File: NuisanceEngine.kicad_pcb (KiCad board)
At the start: 2 copper layers, 60 x 50 mm, 63 parts, among them J1 GND, J2 CV, J3 9V, J4 GND, J5 BAT, J6 L, J7 R, J8 GND, Q1 2N3904, Q2 2N3904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

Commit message: Changed speaker connection
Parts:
- removed LS1: Speaker, Connectors_Molex:Molex_NanoFit_1x02x2.50mm_Straight
- added J10: S-, Connector_PinHeader_2.54mm:PinHeader_1x01_P2.54mm_Vertical, F.Cu at (154.5, 36.8)
- added J9: S+, Connector_PinHeader_2.54mm:PinHeader_1x01_P2.54mm_Vertical, F.Cu at (150.8, 36.8)

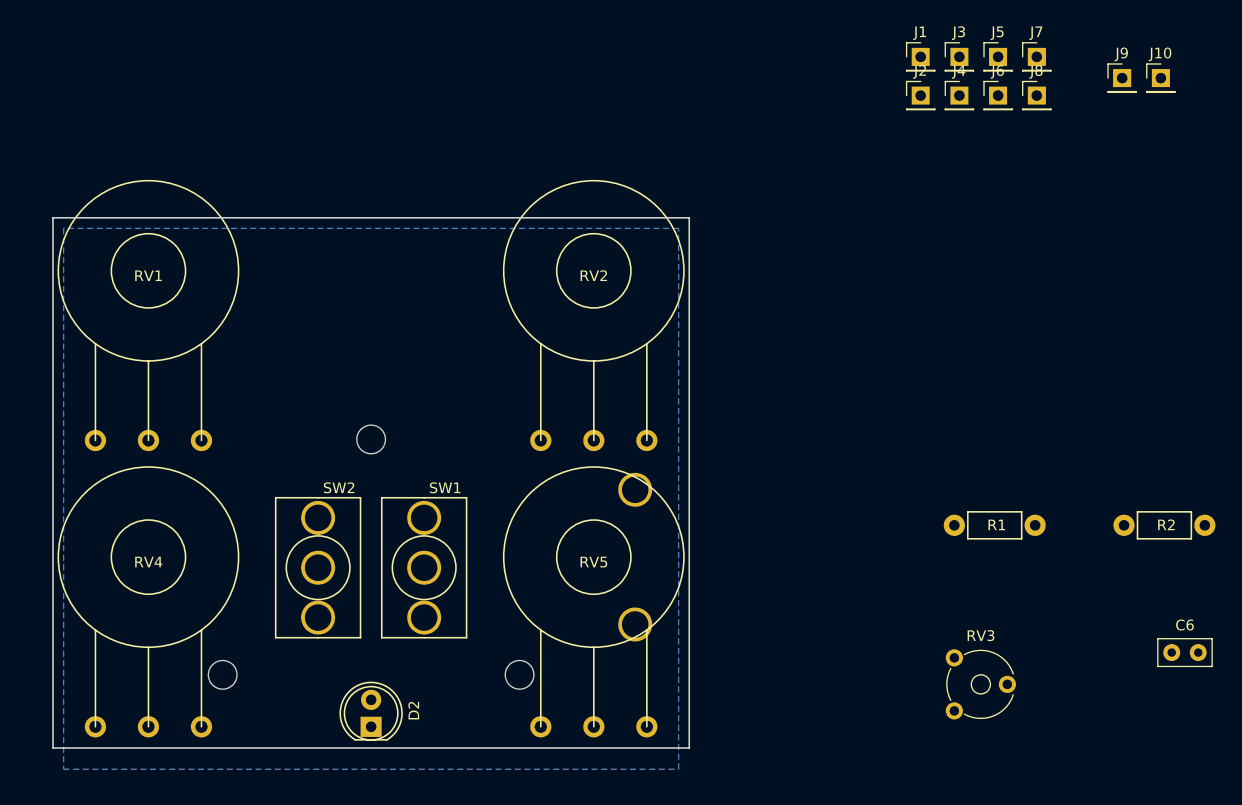
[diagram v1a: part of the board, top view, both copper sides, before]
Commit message: Updated pin headers
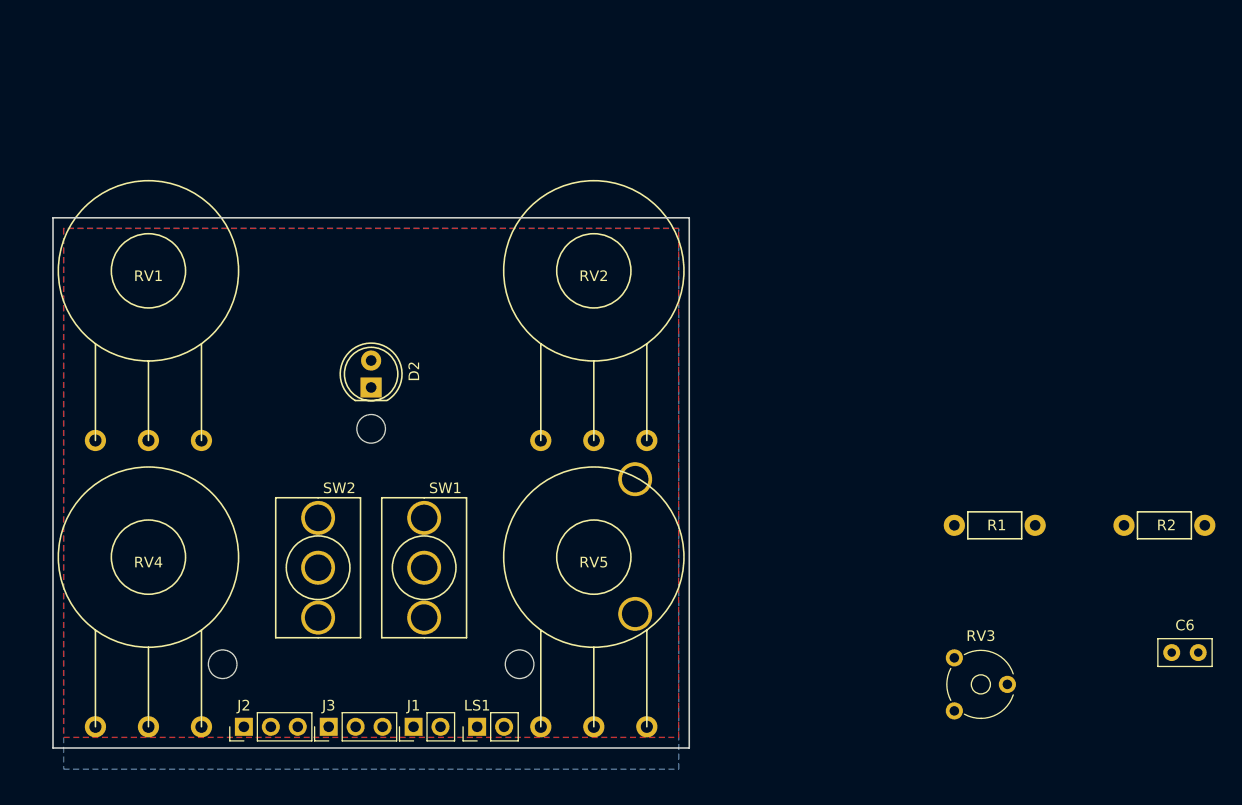
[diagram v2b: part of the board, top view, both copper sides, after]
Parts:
- removed J10: S-, Connector_PinHeader_2.54mm:PinHeader_1x01_P2.54mm_Vertical
- removed J4, J8: GND, Connector_PinHeader_2.54mm:PinHeader_1x01_P2.54mm_Vertical
- removed J5: BAT, Connector_PinHeader_2.54mm:PinHeader_1x01_P2.54mm_Vertical
- removed J6: L, Connector_PinHeader_2.54mm:PinHeader_1x01_P2.54mm_Vertical
- removed J7: R, Connector_PinHeader_2.54mm:PinHeader_1x01_P2.54mm_Vertical
- removed J9: S+, Connector_PinHeader_2.54mm:PinHeader_1x01_P2.54mm_Vertical
- added LS1: Speaker, Connector_PinHeader_2.54mm:PinHeader_1x02_P2.54mm_Vertical, F.Cu at (90.0, 98.0)
- J1: value GND -> CV; footprint Connector_PinHeader_2.54mm:PinHeader_1x01_P2.54mm_Vertical -> Connector_PinHeader_2.54mm:PinHeader_1x02_P2.54mm_Vertical
- J2: value CV -> Headphones; footprint Connector_PinHeader_2.54mm:PinHeader_1x01_P2.54mm_Vertical -> Connector_PinHeader_2.54mm:PinHeader_1x03_P2.54mm_Vertical
- J3: value 9V -> Power; footprint Connector_PinHeader_2.54mm:PinHeader_1x01_P2.54mm_Vertical -> Connector_PinHeader_2.54mm:PinHeader_1x03_P2.54mm_Vertical
- moved J2 87.3 mm to (68.0, 98.0), turned to 90 degrees
- moved J3 86.8 mm to (76.0, 98.0), turned to 90 degrees
- moved J1 79.2 mm to (84.0, 98.0), turned to 90 degrees
- moved D2 32.0 mm to (80.0, 66.0)
- moved BT1 1.00 mm to (80.0, 81.0)
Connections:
- J2 pad 1: Net-(J2-Pad1) -> Net-(C10-Pad1)
- J3 pad 1: Net-(J3-Pad1) -> GND
- R1 pad 1: Net-(J2-Pad1) -> Net-(J1-Pad2)
- SW2 pad 1: Net-(J3-Pad1) -> Net-(J3-Pad2)
- SW2 pad 3: Net-(J3-Pad1) -> Net-(J3-Pad2)
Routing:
- added copper zone on F.Cu, net GND

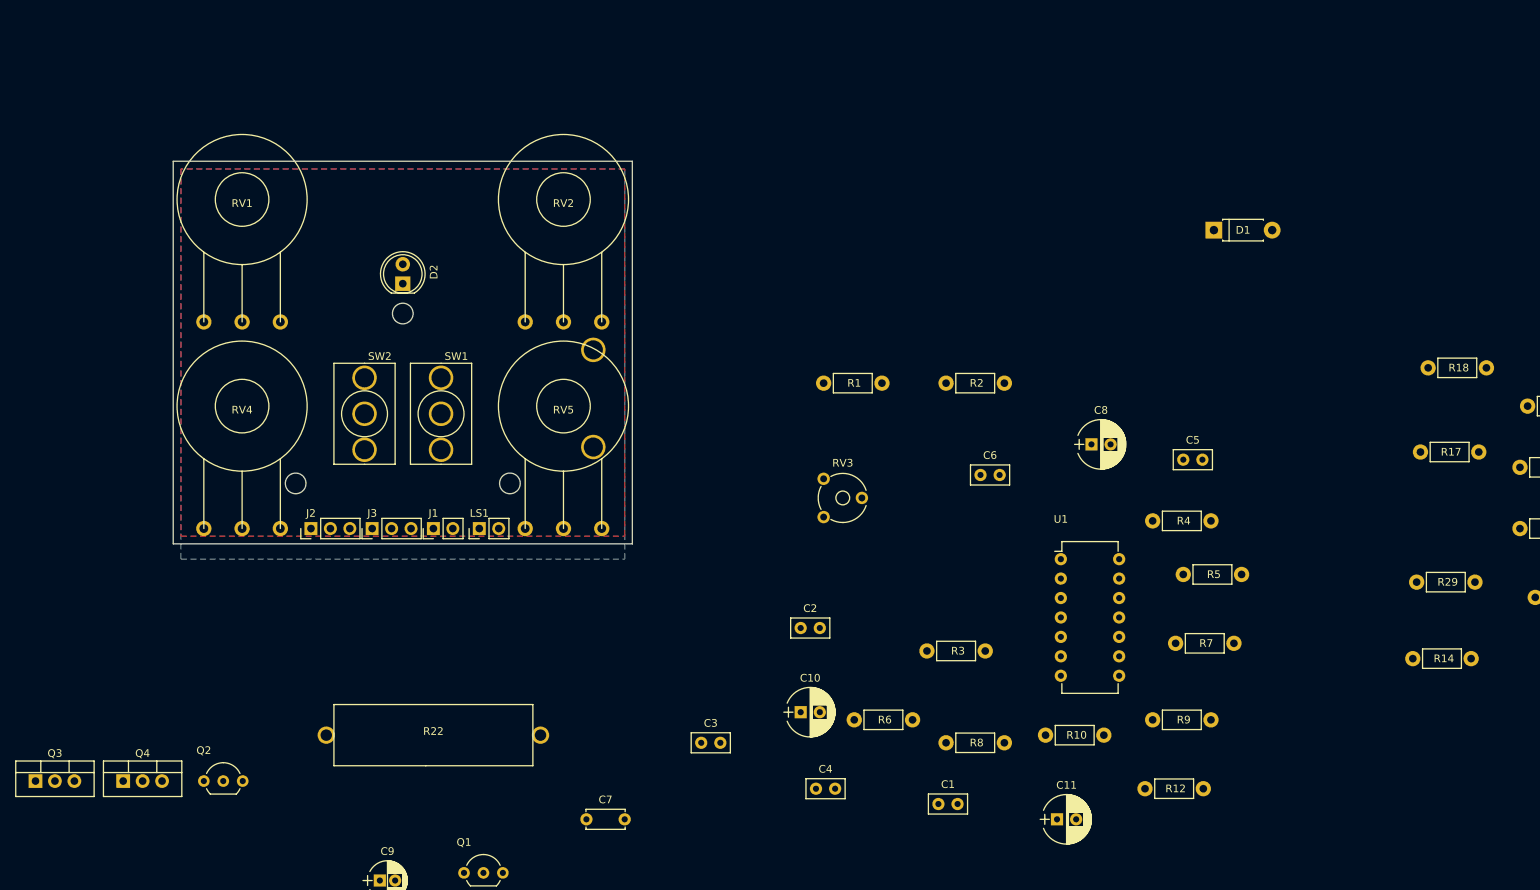
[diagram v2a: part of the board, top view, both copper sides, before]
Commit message: Started basic layout
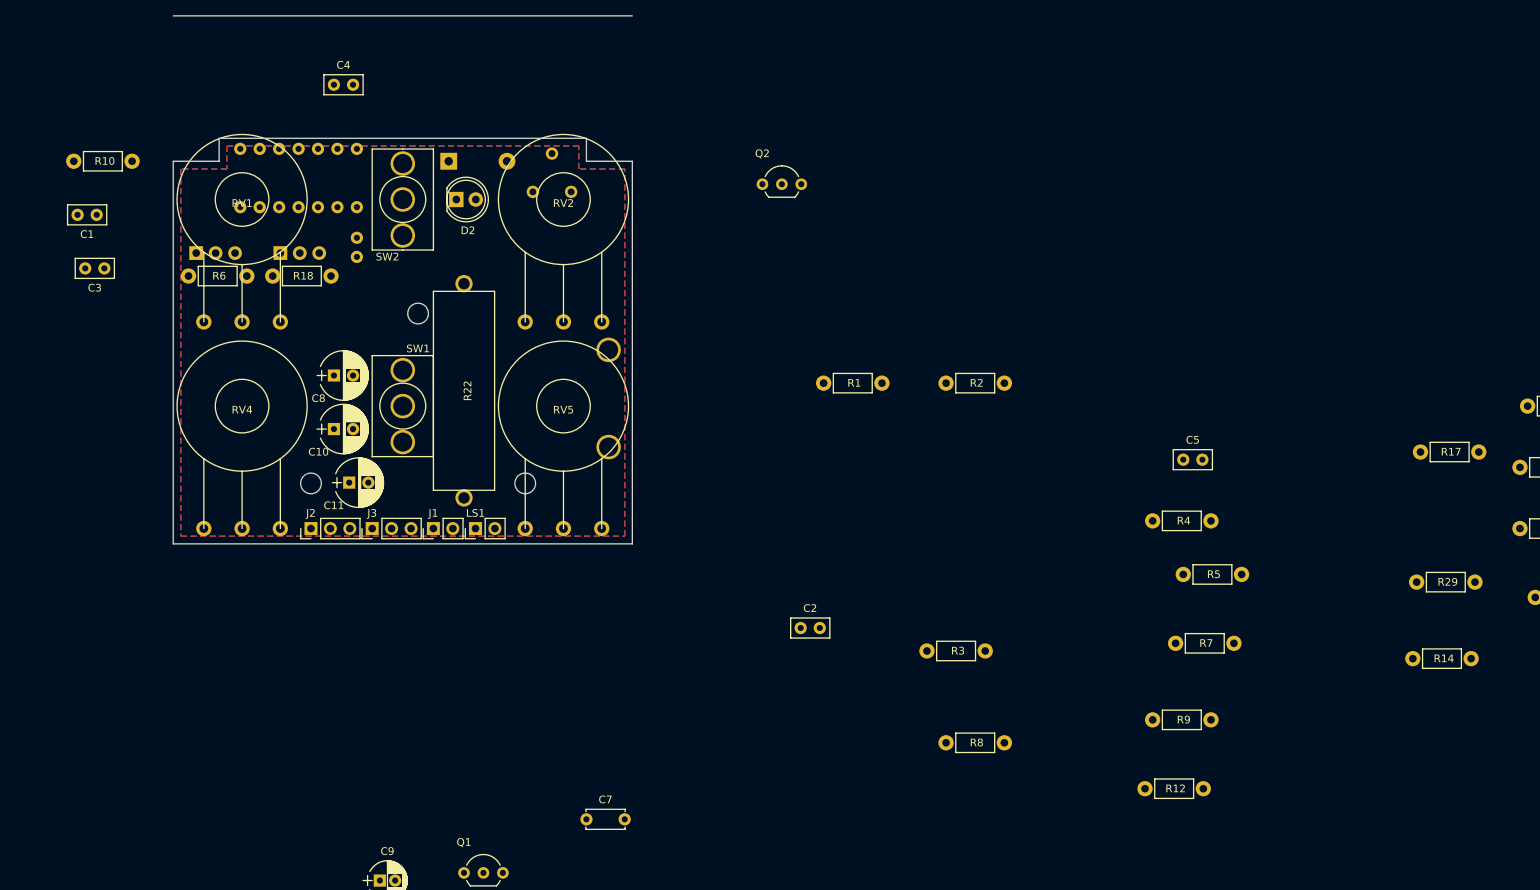
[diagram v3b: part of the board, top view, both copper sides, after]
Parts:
- C6, D1, Q3, Q4, RV3, U1: moved to B.Cu
- moved R18 151.5 mm to (63.0, 65.0)
- moved R10 147.5 mm to (37.0, 50.0)
- moved C1 134.3 mm to (40.0, 57.0), turned to 180 degrees
- moved C4 111.5 mm to (71.0, 40.0)
- moved Q2 106.8 mm to (127.0, 53.0)
- moved R6 104.6 mm to (52.0, 65.0)
- moved U1 102.9 mm to (74.0, 56.0), turned to 90 degrees
- moved C11 102.4 mm to (73.0, 92.0)
- moved D1 100.4 mm to (86.0, 50.0)
- moved C3 99.6 mm to (41.0, 64.0), turned to 180 degrees
- moved C8 99.4 mm to (71.0, 78.0)
- moved C6 87.2 mm to (74.0, 60.0), turned to 270 degrees
- moved Q3 76.1 mm to (64.0, 62.0)
- moved C10 71.3 mm to (71.0, 85.0)
- moved Q4 69.7 mm to (53.0, 62.0)
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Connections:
- SW2 pad 3: Net-(J3-Pad2) -> Net-(SW2-Pad3)
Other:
- board size 60 x 50 mm -> 60 x 69 mm

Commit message: More mushing. Gonna be a mushy one haha
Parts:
- C1, C3, C5: moved to B.Cu
- moved R25 208.4 mm to (44.0, 109.0)
- moved R13 196.0 mm to (39.0, 55.0)
- moved R29 195.9 mm to (37.0, 18.0)
- moved R27 193.0 mm to (70.0, 108.0)
- moved R26 189.1 mm to (66.0, 108.0), turned to 180 degrees
- moved R11 175.8 mm to (52.0, 65.0)
- moved R16 175.5 mm to (52.0, 95.0)
- moved R24 175.0 mm to (70.6, 68.0), turned to 180 degrees
- moved R7 166.5 mm to (39.0, 26.0), turned to 180 degrees
- moved R9 165.6 mm to (50.0, 18.0)
- moved R14 163.4 mm to (77.0, 23.0)
- moved R15 136.4 mm to (90.0, 108.0), turned to 180 degrees
- moved C5 133.6 mm to (52.0, 58.0)
- moved R23 133.4 mm to (123.0, 53.0)
- moved Q1 127.4 mm to (69.0, 17.0)
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
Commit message: More mushing
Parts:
- C10, C11: footprint Capacitors_THT:CP_Radial_D6.3mm_P2.50mm -> Capacitor_THT:CP_Radial_D5.0mm_P2.00mm
- C4, C9, R3: moved to B.Cu
- C8: footprint Capacitors_THT:CP_Radial_D6.3mm_P2.50mm -> Capacitor_THT:CP_Radial_D6.3mm_P2.50mm
- moved R6 96.5 mm to (135.5, 76.5)
- moved R2 71.1 mm to (64.0, 74.5)
- moved R5 66.2 mm to (74.5, 74.0), turned to 90 degrees
- moved R13 62.8 mm to (100.5, 67.5)
- moved C9 61.4 mm to (92.0, 50.0), turned to 0 degrees
- moved R15 53.4 mm to (51.5, 71.0), turned to 270 degrees
- moved R9 53.0 mm to (27.5, 66.0)
- moved R12 49.9 mm to (77.5, 66.5), turned to 270 degrees
- moved R3 38.2 mm to (93.0, 60.0)
- moved R25 26.2 mm to (64.0, 92.0), turned to 180 degrees
- moved R27 23.9 mm to (74.5, 84.5), turned to 180 degrees
- moved R11 22.5 mm to (51.5, 87.5), turned to 270 degrees
- moved R26 22.2 mm to (74.5, 87.5)
- moved C4 20.7 mm to (91.0, 36.5)
- moved D1 16.0 mm to (77.5, 63.5)
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
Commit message: Commit before trying smt
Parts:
- R17, R6, R9: moved to B.Cu
- moved R1 81.0 mm to (100.0, 95.0)
- moved R9 80.5 mm to (108.0, 64.0), turned to 180 degrees
- moved R23 50.2 mm to (100.0, 92.0)
- moved R6 49.4 mm to (88.0, 63.0), turned to 0 degrees
- moved Q1 47.2 mm to (94.0, 57.0)
- moved R17 33.2 mm to (108.0, 61.0), turned to 180 degrees
- moved C4 15.3 mm to (86.0, 51.0), turned to 90 degrees
- moved Q2 11.7 mm to (108.0, 56.0)
- moved RV3 3.16 mm to (94.0, 53.0)
- moved C9 3.00 mm to (89.0, 50.0)

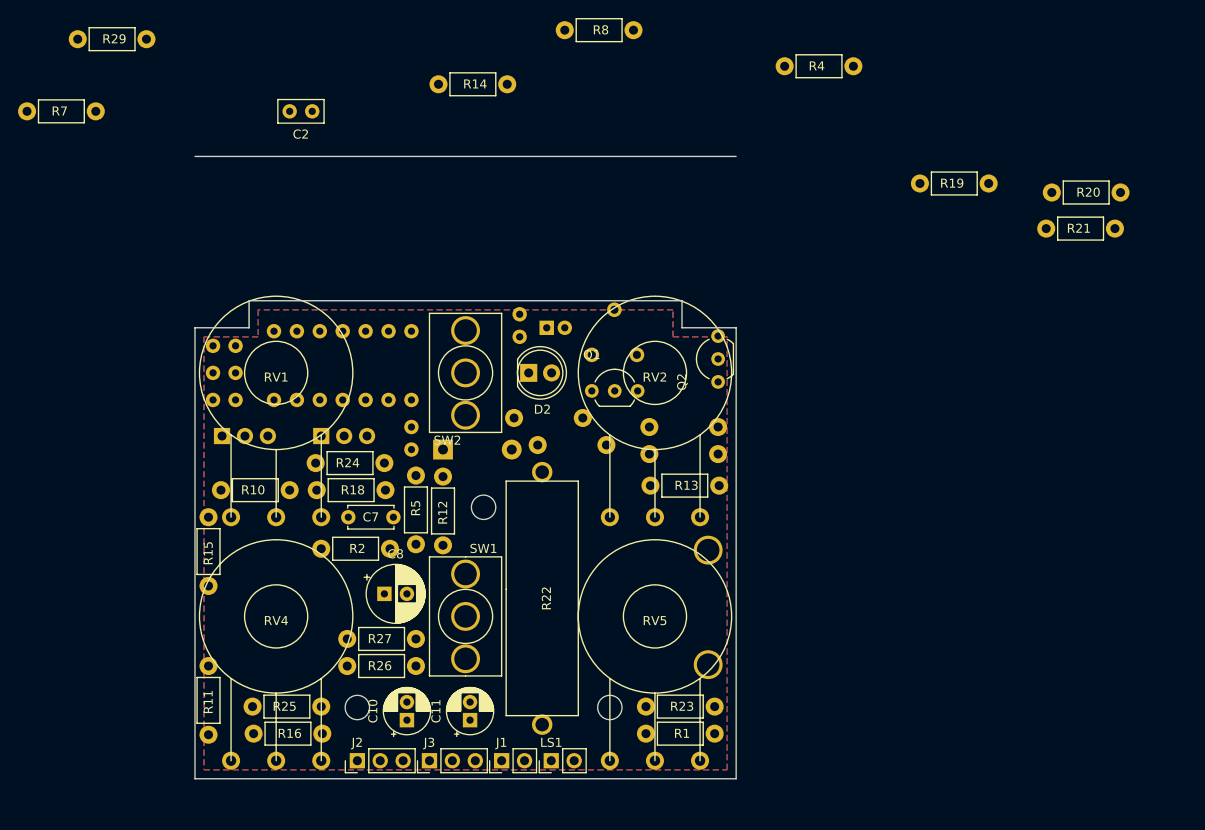
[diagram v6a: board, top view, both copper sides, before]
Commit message: Switched to SMT footprints
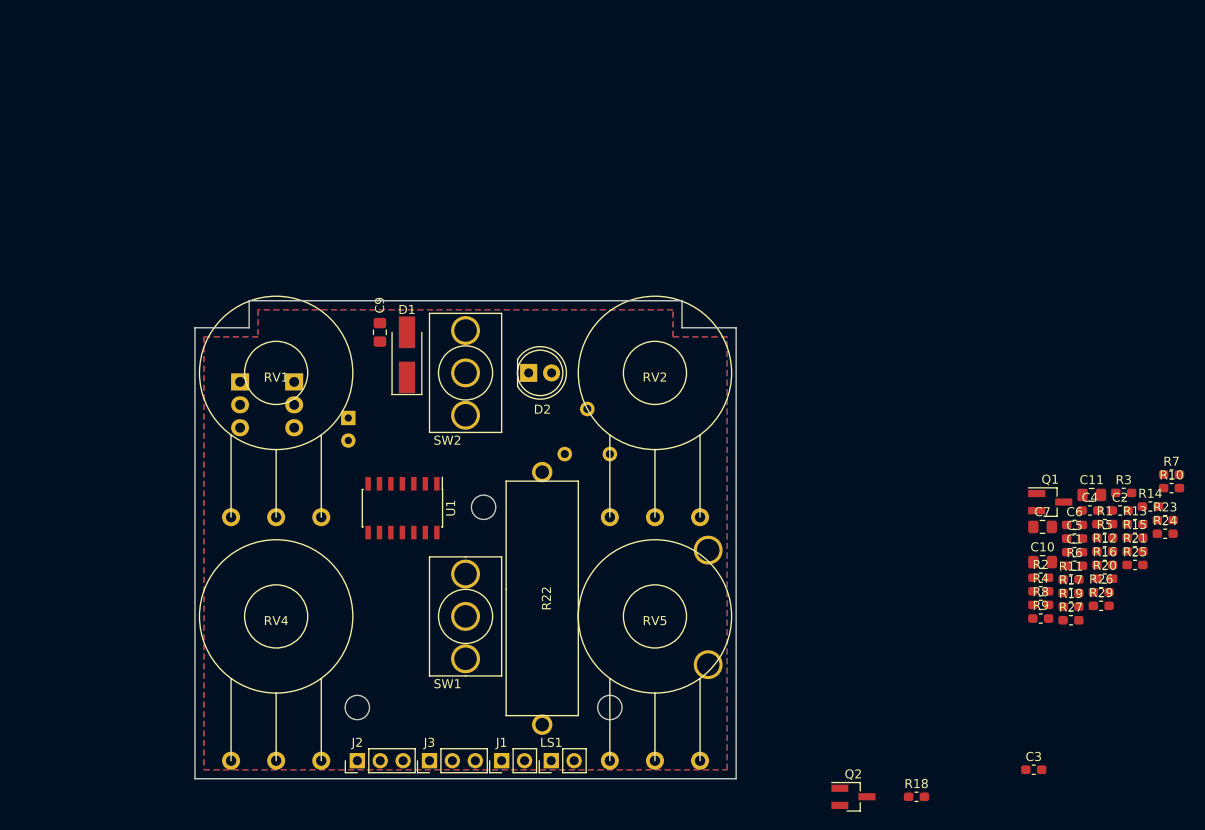
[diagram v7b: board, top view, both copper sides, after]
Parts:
- C1, C3, C4, C5, C6: footprint Capacitors_THT:C_Disc_D5.0mm_W2.5mm_P2.50mm -> Capacitor_SMD:C_0603_1608Metric_Pad1.05x0.95mm_HandSolder; moved to F.Cu
- C10, C11: footprint Capacitor_THT:CP_Radial_D5.0mm_P2.00mm -> Resistor_SMD:R_0805_2012Metric_Pad1.15x1.40mm_HandSolder
- C2: footprint Capacitors_THT:C_Disc_D5.0mm_W2.5mm_P2.50mm -> Capacitor_SMD:C_0603_1608Metric_Pad1.05x0.95mm_HandSolder
- C7: footprint Capacitors_THT:C_Disc_D5.0mm_W2.5mm_P5.00mm -> Capacitor_SMD:C_0805_2012Metric_Pad1.15x1.40mm_HandSolder
- C8: moved to B.Cu
- C9: footprint Capacitors_THT:CP_Radial_D5.0mm_P2.00mm -> Resistor_SMD:R_0805_2012Metric_Pad1.15x1.40mm_HandSolder; moved to F.Cu
- D1: footprint Diodes_THT:D_DO-41_SOD81_P7.62mm_Horizontal -> Diode_SMD:D_SMA_Handsoldering; moved to F.Cu
- Q1, Q2: footprint TO_SOT_Packages_THT:TO-92_Inline_Wide -> Package_TO_SOT_SMD:SOT-23_Handsoldering
- Q3, Q4: footprint TO_SOT_Packages_THT:TO-220_Vertical -> Package_TO_SOT_THT:TO-220-3_Vertical
- R1, R10, R11, R12, R13, R14, R15, R16, R18, R19, R2, R20, R21, R23, R24, R25, R26, R27, R29, R4, R5, R7, R8: footprint Resistors_THT:Resistor_Horizontal_RM7mm -> Resistor_SMD:R_0603_1608Metric_Pad1.05x0.95mm_HandSolder
- R17, R3, R6, R9: footprint Resistors_THT:Resistor_Horizontal_RM7mm -> Resistor_SMD:R_0603_1608Metric_Pad1.05x0.95mm_HandSolder; moved to F.Cu
- U1: footprint Housings_DIP:DIP-14_W7.62mm -> Package_SO:SOIC-14_3.9x8.7mm_P1.27mm; moved to F.Cu
- moved R29 129.7 mm to (150.5, 80.8)
- moved R7 125.9 mm to (158.3, 66.3), turned to 0 degrees
- moved R15 102.8 mm to (154.2, 73.3), turned to 0 degrees
- moved C2 99.9 mm to (152.6, 70.3), turned to 0 degrees
- moved C3 98.8 mm to (143.0, 99.0), turned to 0 degrees
- moved C1 98.2 mm to (147.5, 74.9)
- moved R10 97.8 mm to (158.3, 67.8), turned to 0 degrees
- moved C5 96.8 mm to (147.5, 73.4)
- moved R16 96.2 mm to (150.9, 76.3)
- moved R11 96.1 mm to (147.1, 77.9), turned to 0 degrees
- moved R14 91.8 mm to (155.9, 69.8)
- moved R25 91.6 mm to (154.2, 76.3), turned to 0 degrees
- moved R24 86.9 mm to (157.6, 72.8), turned to 0 degrees
- moved R8 82.7 mm to (143.8, 80.7)
- moved R2 79.8 mm to (143.8, 77.7)
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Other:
- board size 60 x 69 mm -> 60 x 53 mm

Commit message: Spread components:
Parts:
- D1: footprint Diode_SMD:D_SMA_Handsoldering -> Diode_THT:D_DO-41_SOD81_P7.62mm_Horizontal
- moved R1 92.2 mm to (59.0, 79.0), turned to 90 degrees
- moved R24 90.7 mm to (69.0, 53.5), turned to 270 degrees
- moved R16 90.6 mm to (61.0, 65.0)
- moved R25 90.3 mm to (68.0, 49.5), turned to 180 degrees
- moved R12 89.3 mm to (62.0, 83.0), turned to 270 degrees
- moved R5 89.1 mm to (62.0, 78.9), turned to 270 degrees
- moved C2 88.6 mm to (65.0, 57.0), turned to 270 degrees
- moved R13 87.8 mm to (67.0, 62.0), turned to 270 degrees
- moved R7 85.4 mm to (73.0, 61.0), turned to 270 degrees
- moved R21 85.2 mm to (69.0, 76.0), turned to 90 degrees
- moved R2 84.8 mm to (59.0, 75.0), turned to 270 degrees
- moved R4 81.9 mm to (62.0, 75.1), turned to 90 degrees
- moved C5 81.8 mm to (66.0, 67.0), turned to 180 degrees
- moved R9 81.3 mm to (65.0, 62.0), turned to 90 degrees
- moved C11 80.9 mm to (72.5, 93.5)
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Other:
- board text added: "9V"
- board text added: "BAT"
- board text added: "CV"
- board text added: "GND"
- board text added: "JL"
- board text added: "JR"
- board text added: "SPK"
